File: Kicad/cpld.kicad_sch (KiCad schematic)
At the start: 16 parts, among them J2 Conn_01x06_Pin, U7 AMS1117-3.3, U9 XC95144XL-TQ144

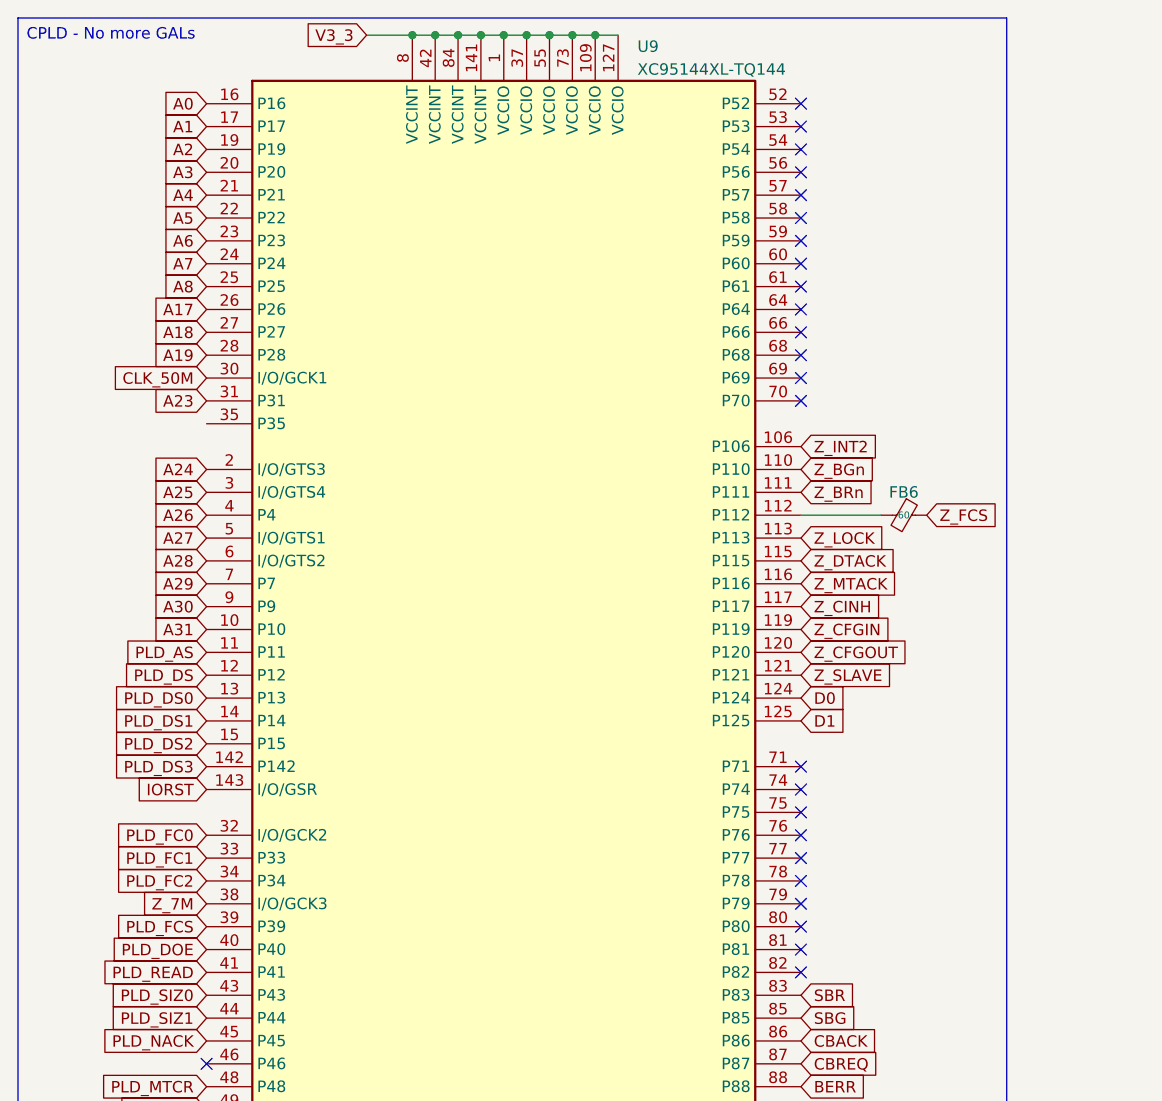
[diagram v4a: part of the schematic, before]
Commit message: Clean up CPLD signals / prepare for rotation
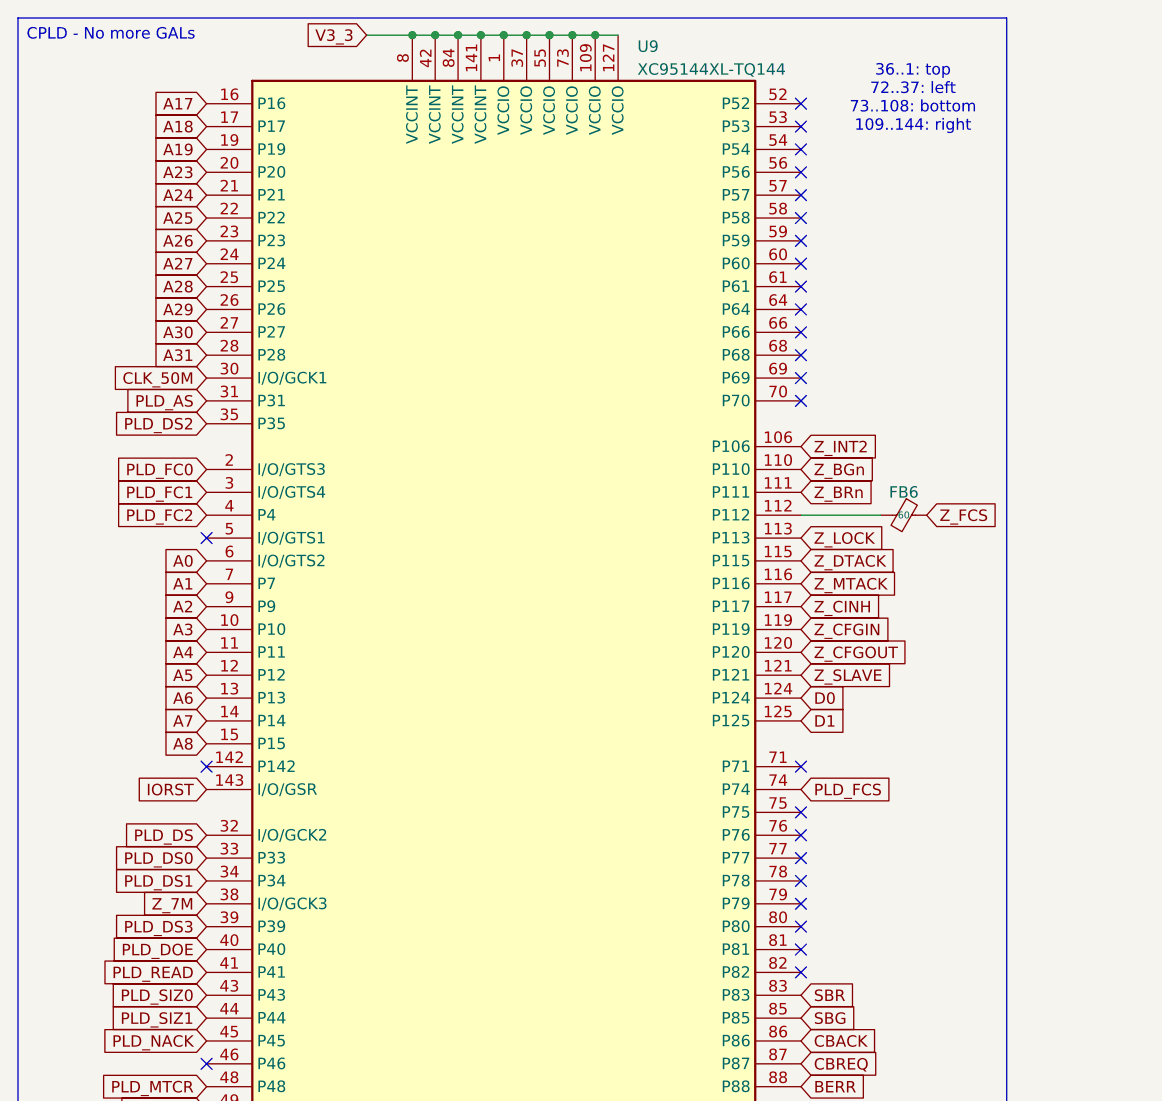
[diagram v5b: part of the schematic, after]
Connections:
- net A0: now also U9.6 (I/O/GTS2); no longer U9.16 (P16)
- net A1: now also U9.7 (P7); no longer U9.17 (P17)
- net A17: now also U9.16 (P16); no longer U9.26 (P26)
- net A18: now also U9.17 (P17); no longer U9.27 (P27)
- net A19: now also U9.19 (P19); no longer U9.28 (P28)
- net A2: now also U9.9 (P9); no longer U9.19 (P19)
- net A23: now also U9.20 (P20); no longer U9.31 (P31)
- net A24: now also U9.21 (P21); no longer U9.2 (I/O/GTS3)
- net A25: now also U9.22 (P22); no longer U9.3 (I/O/GTS4)
- net A26: now also U9.23 (P23); no longer U9.4 (P4)
- net A27: now also U9.24 (P24); no longer U9.5 (I/O/GTS1)
- net A28: now also U9.25 (P25); no longer U9.6 (I/O/GTS2)
- net A29: now also U9.26 (P26); no longer U9.7 (P7)
- net A3: now also U9.10 (P10); no longer U9.20 (P20)
- net A30: now also U9.27 (P27); no longer U9.9 (P9)
- net A31: now also U9.28 (P28); no longer U9.10 (P10)
- net A4: now also U9.11 (P11); no longer U9.21 (P21)
- net A5: now also U9.12 (P12); no longer U9.22 (P22)
- net A6: now also U9.13 (P13); no longer U9.23 (P23)
- net A7: now also U9.14 (P14); no longer U9.24 (P24)
- net A8: now also U9.15 (P15); no longer U9.25 (P25)
- net PLD_AS: now also U9.31 (P31); no longer U9.11 (P11)
- net PLD_DS: now also U9.32 (I/O/GCK2); no longer U9.12 (P12)
- net PLD_DS0: now also U9.33 (P33); no longer U9.13 (P13)
- net PLD_DS1: now also U9.34 (P34); no longer U9.14 (P14)
- net PLD_DS2: now also U9.35 (P35); no longer U9.15 (P15)
- net PLD_DS3: now also U9.39 (P39); no longer U9.142 (P142)
- net PLD_FC0: now also U9.2 (I/O/GTS3); no longer U9.32 (I/O/GCK2)
- net PLD_FC1: now also U9.3 (I/O/GTS4); no longer U9.33 (P33)
- net PLD_FC2: now also U9.4 (P4); no longer U9.34 (P34)
- net PLD_FCS: now also U9.74 (P74); no longer U9.39 (P39)
- no-connect marks 30 -> 31
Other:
- note added: "36..1: top 72..37: left 73..108: bottom 109..144: right"

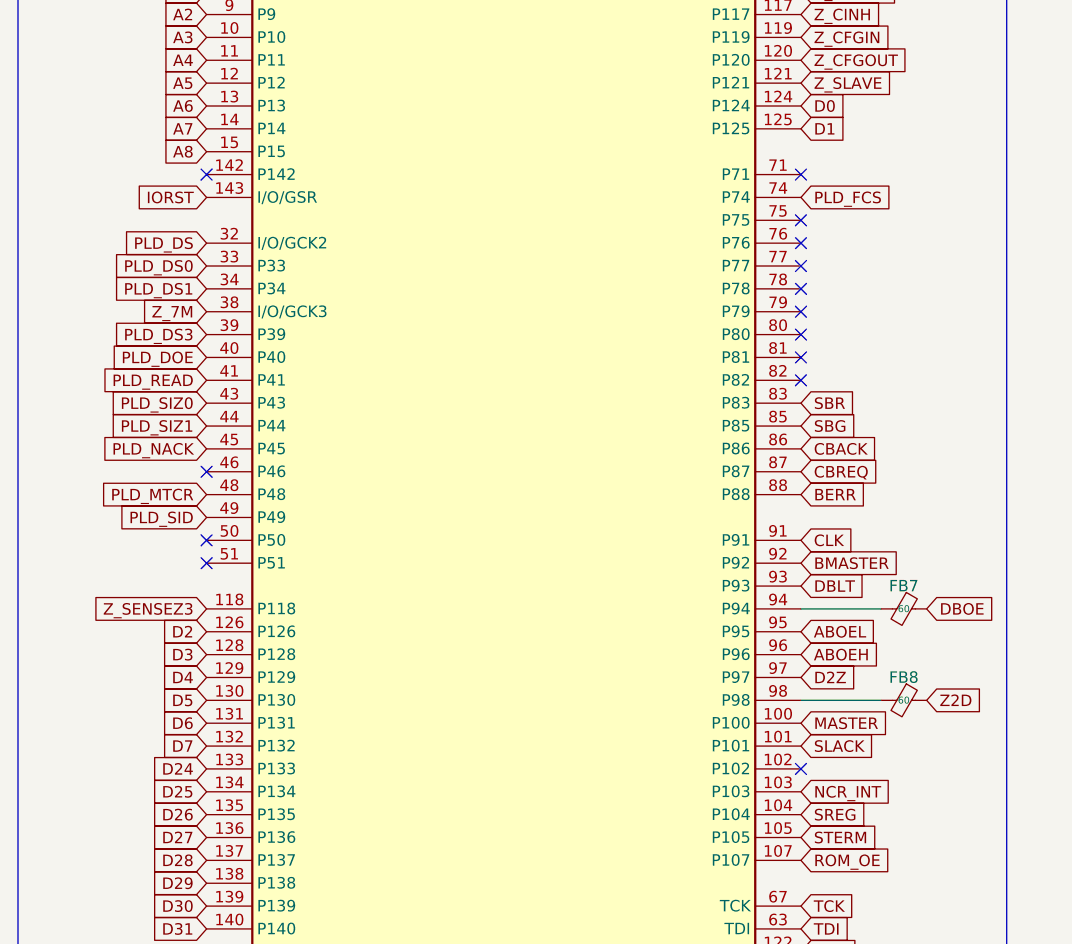
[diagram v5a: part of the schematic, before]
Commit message: ROM_WE Single net Issue #3
Connect ROM_WE to CPLD. Also connect ROM_CE.
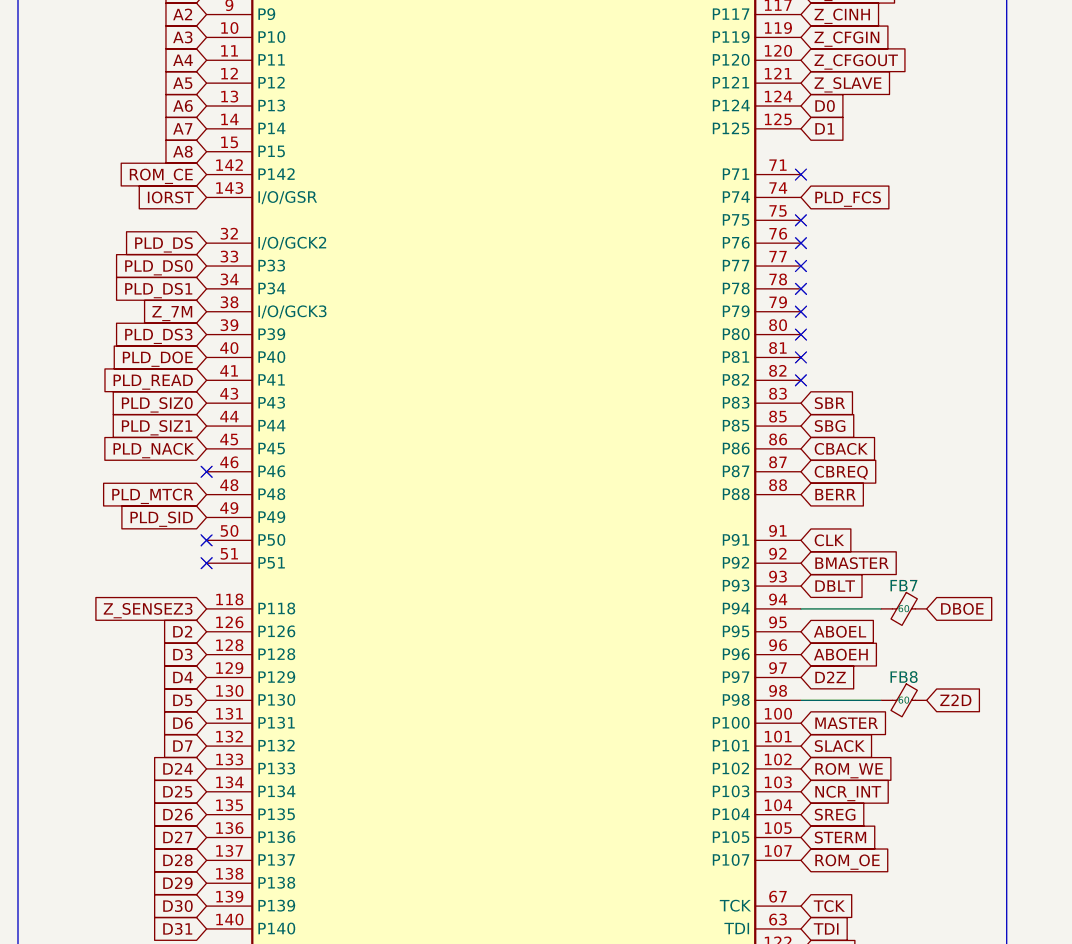
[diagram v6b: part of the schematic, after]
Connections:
- net ROM_WE: now reaches U9.102 (P102)
- net ROM_CE: now reaches U9.142 (P142)
- no-connect marks 31 -> 29
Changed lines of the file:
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@@
-	)
-	(no_connect
-		(at 34.29 96.52)
 	)
 	(no_connect
@@
 	)
 	(no_connect
-		(at 100.33 162.56)
-	)
-	(no_connect
 		(at 100.33 45.72)
 	)
@@
 		)
 	)
+	(global_label "ROM_CE"
+		(shape input)
+		(at 34.29 96.52 180)
+		(fields_autoplaced yes)
+		(effects
+			(font
+				(size 1.27 1.27)
+			)
+			(justify right)
+		)
+		(property "Intersheetrefs" "${INTERSHEET_REFS}"
+			(at 23.8663 96.52 0)
+			(effects
+				(font
+					(size 1.27 1.27)
+				)
+				(justify right)
+				(hide yes)
+			)
+		)
+	)
 	(global_label "A18"
 		(shape input)
@@
 			(effects
 				(font
+					(size 1.27 1.27)
+				)
+				(justify left)
+				(hide yes)
+			)
+		)
+	)
+	(global_label "ROM_WE"
+		(shape input)
+		(at 100.33 162.56 0)
+		(fields_autoplaced yes)
+		(effects
+			(font
+				(size 1.27 1.27)
+			)
+			(justify left)
+		)
+		(property "Intersheetrefs" "${INTERSHEET_REFS}"
+			(at 110.9351 162.56 0)
+			(effects
+				(font
